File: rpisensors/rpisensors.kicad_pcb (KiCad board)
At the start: 2 copper layers, 8 parts, among them J1 Conn_02x20_Odd_Even, J2 Conn_01x08_Male, J3 Conn_01x08_Male, J4 Conn_01x08_Male, J5 Conn_01x08_Male, J6 Conn_01x08_Male, J7 Conn_01x08_Male

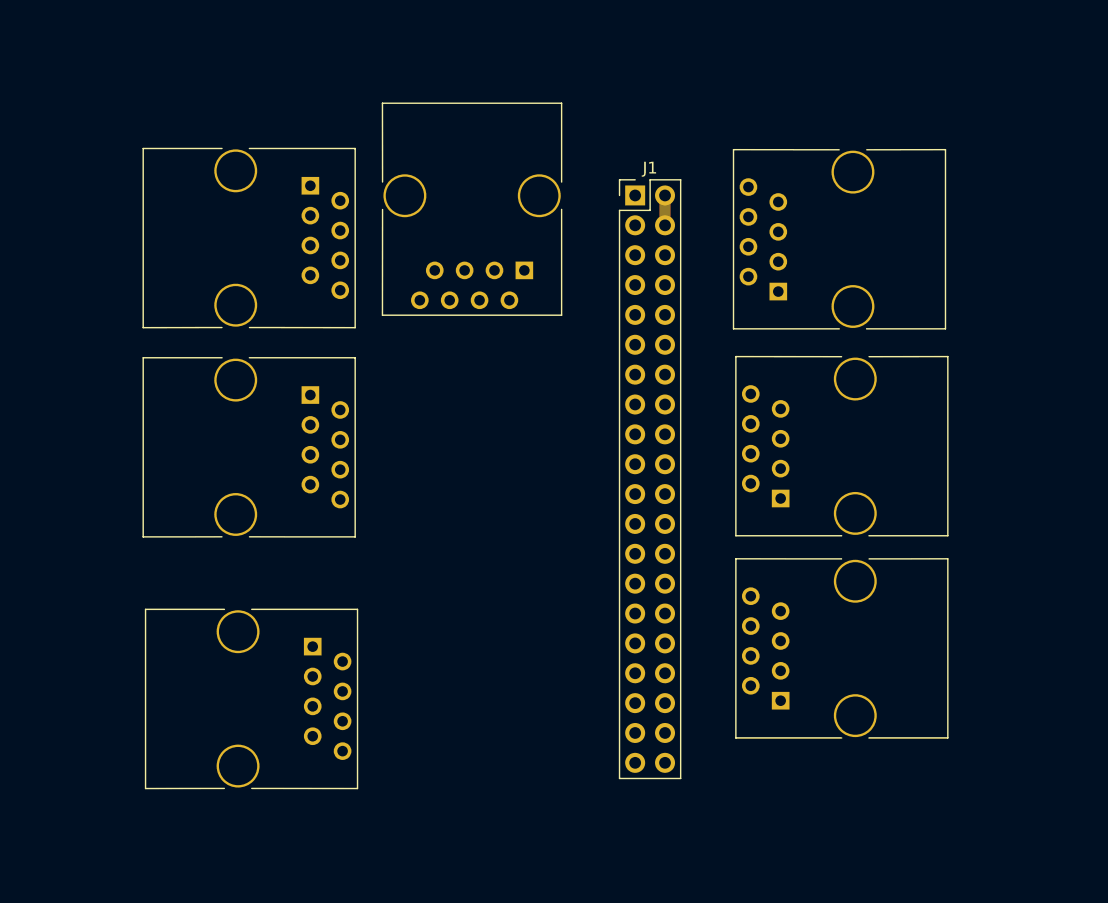
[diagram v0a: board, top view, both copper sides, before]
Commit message: Added wiring. Lacks silkscreen and final touch
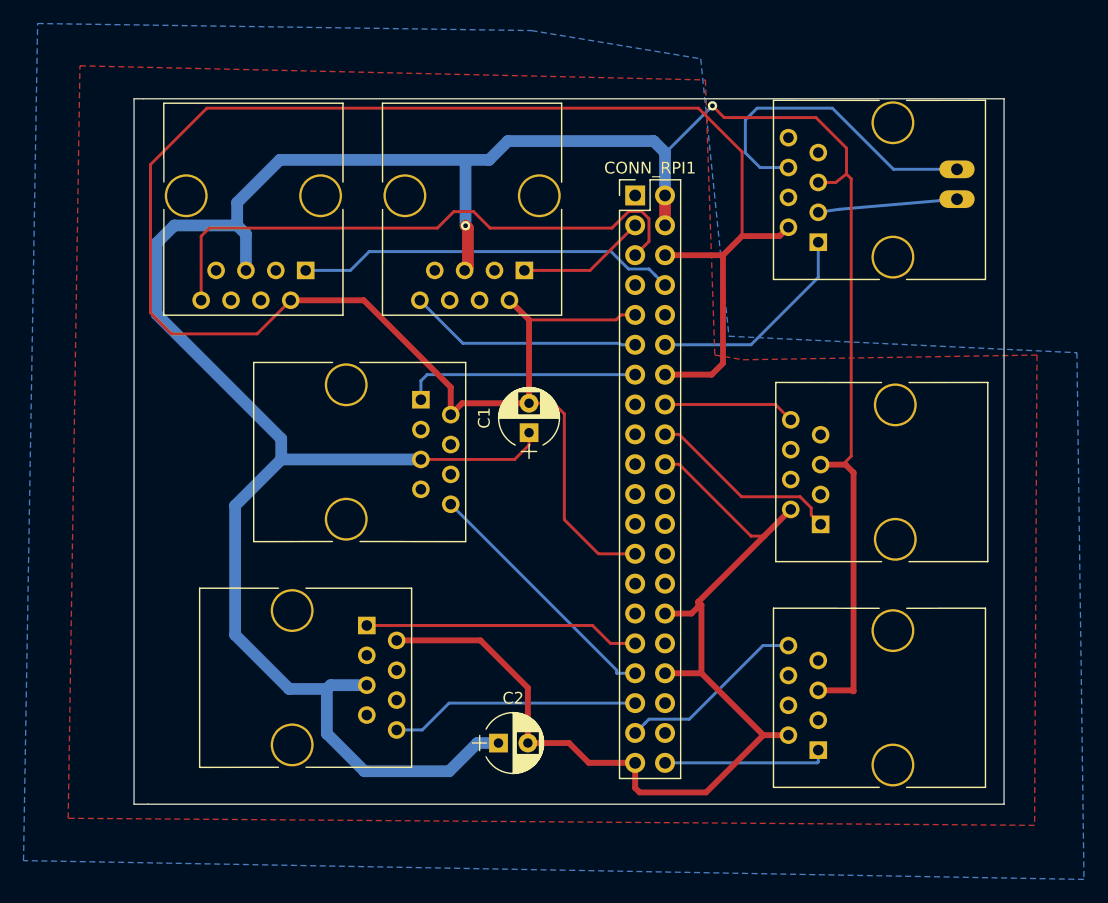
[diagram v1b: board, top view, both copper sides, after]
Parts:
- removed J2: Conn_01x08_Male, rj45:RJ45_8_Stewart_2891016
- added C1: 10uF, Capacitors_THT:CP_Radial_D5.0mm_P2.50mm, F.Cu at (82.8, 82.4)
- added C2: 10uF, Capacitors_THT:CP_Radial_D5.0mm_P2.50mm, F.Cu at (80.2, 108.8)
- added CONN1: Conn_01x08_Male, rj45:RJ45_8_Stewart_2891016, F.Cu at (82.4, 68.6)
- added J1: Conn_01x02_Male, Connectors:PINHEAD1-2, B.Cu at (119.2, 60.0)
- moved CONN5 52.7 mm to (107.4, 109.4), turned to 90 degrees
- moved CONN6 44.4 mm to (107.6, 90.2), turned to 90 degrees
- moved CONN4 35.8 mm to (69.0, 98.8), turned to 270 degrees
- moved CONN3 31.8 mm to (73.6, 79.6), turned to 270 degrees
- moved HAN1 22.0 mm to (107.4, 66.2)
- moved CONN2 7.21 mm to (63.8, 68.6), turned to 180 degrees
- renumbered J3 to CONN2, J4 to CONN3, J5 to CONN4, J6 to CONN5, HAN++1 to CONN6, J1 to CONN_RPI1, J7 to HAN1
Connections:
- CONN2 pad 1: Net-(J3-Pad1) -> /SENSOR_2
- CONN2 pad 2: Net-(J3-Pad2) -> GND
- CONN2 pad 5: Net-(J3-Pad5) -> +5V
- CONN2 pad 8: Net-(J3-Pad8) -> /ACT_2
- CONN3 pad 1: Net-(J4-Pad1) -> /GPIO27
- CONN3 pad 2: Net-(J4-Pad2) -> GND
- CONN3 pad 5: Net-(J4-Pad5) -> +5V
- CONN3 pad 8: Net-(J4-Pad8) -> /ACT_3
- CONN4 pad 1: Net-(J5-Pad1) -> /GPIO6
- CONN4 pad 2: Net-(J5-Pad2) -> GND
- CONN4 pad 5: Net-(J5-Pad5) -> +5V
- CONN4 pad 8: Net-(J5-Pad8) -> /ACT_4
- CONN5 pad 1: Net-(J6-Pad1) -> /GPIO21
- CONN5 pad 2: Net-(J6-Pad2) -> GND
- CONN5 pad 5: Net-(J6-Pad5) -> +5V
- CONN5 pad 8: Net-(J6-Pad8) -> /ACT_5
- CONN6 pad 1: Net-(HAN++1-Pad1) -> /GPIO24
- CONN6 pad 2: Net-(HAN++1-Pad2) -> GND
- CONN6 pad 5: Net-(HAN++1-Pad5) -> +5V
- CONN6 pad 8: Net-(HAN++1-Pad8) -> /ACT_6
- CONN_RPI1 pad 11: /GPIO17 -> /ACT_1
- CONN_RPI1 pad 16: /GPIO23 -> /ACT_6
- CONN_RPI1 pad 33: /GPIO13 -> /ACT_3
- CONN_RPI1 pad 35: /GPIO19 -> /ACT_4
- CONN_RPI1 pad 37: /GPIO26 -> /ACT_5
- CONN_RPI1 pad 5: /GPIO3 -> /ACT_2
- CONN_RPI1 pad 8: /UART0_TX -> /SENSOR_2
- HAN1 pad 1: Net-(J7-Pad1) -> /GPIO18
- HAN1 pad 2: Net-(J7-Pad2) -> GND
- HAN1 pad 3: Net-(J7-Pad3) -> /HAN+
- HAN1 pad 5: Net-(J7-Pad5) -> +5V
- HAN1 pad 6: Net-(J7-Pad6) -> /HAN-
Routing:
- net GND: track 0.00 -> 264.8 mm
- net +5V: track 2.54 -> 239.4 mm, vias 0 -> 2
- net /ACT_2: track 0.00 -> 49.4 mm
- net /SENSOR_2: track 0.00 -> 32.4 mm
- net /HAN-: track 0.00 -> 27.5 mm
- net /GPIO6: track 0.00 -> 23.5 mm
- net /ACT_3: track 0.00 -> 21.8 mm
- net /ACT_4: track 0.00 -> 21.2 mm
- net /GPIO27: track 0.00 -> 20.0 mm
- net /ACT_1: track 0.00 -> 19.9 mm
- net /GPIO18: track 0.00 -> 18.4 mm
- net /GPIO24: track 0.00 -> 16.8 mm
- net /ACT_5: track 0.00 -> 16.1 mm
- net /GPIO21: track 0.00 -> 14.1 mm
- net /HAN+: track 0.00 -> 11.9 mm
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- added copper zone on B.Cu, net +5V
- added copper zone on F.Cu, net GND
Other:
- board outline added: 74 x 60 mm
